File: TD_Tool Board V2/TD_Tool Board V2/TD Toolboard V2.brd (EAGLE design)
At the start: 8.6 x 5 mm, 142 parts, among them J3 430450400CON_430450400_MOL, M1 NMOSFET_WSD3066DN33, M2 CJ3400, M3 CJ3400, M4 CJ3400, P1 TPS54202_BUCKCONV, P2 3.3V, U1 RP2040IC57_RP2040-L, U2 W25Q128JVSIQSOIC_128JVSIQ_WIN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, U3 SN65HVD1050DRD8-L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

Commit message: Buck Converter Routing
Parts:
- moved 24V 128.3 mm to (92.2, -44.0)
- moved 5V 128.2 mm to (92.2, -41.8)
- moved R8 100.6 mm to (109.4, -43.4), turned to 0 degrees
- moved R9 99.6 mm to (109.4, -42.0), turned to 180 degrees
- moved R7 92.7 mm to (110.9, -44.6), turned to 0 degrees
- moved C21 46.2 mm to (111.7, -39.4), turned to 90 degrees
- moved J1 44.6 mm to (97.6, -43.9), turned to 90 degrees
- moved C22 43.4 mm to (111.8, -42.5), turned to 90 degrees
- moved C19 42.7 mm to (100.1, -42.2), turned to 90 degrees
- moved L1 42.6 mm to (105.9, -36.3), turned to 0 degrees
- moved C18 41.1 mm to (101.5, -42.3), turned to 90 degrees
- moved R6 41.0 mm to (102.7, -40.8), turned to 90 degrees
- moved R5 38.7 mm to (102.6, -44.4), turned to 90 degrees
- moved P1 36.0 mm to (106.3, -42.7), turned to 0 degrees
- moved C20 34.9 mm to (108.5, -40.7), turned to 0 degrees
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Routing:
- net GND: track 0.00 -> 35.6 mm, vias 0 -> 4
- net +5V: track 0.00 -> 15.7 mm
- net +24V: track 0.00 -> 15.7 mm
- net VREGO: track 0.00 -> 14.0 mm, vias 0 -> 8
- net VREGEN: track 0.00 -> 10.1 mm, vias 0 -> 3
- net VREGFB: track 0.00 -> 3.90 mm
- net VRC: track 0.00 -> 2.93 mm
- net BCBOOT: track 0.00 -> 1.13 mm
- added copper zone on layer 1, net +24V
- added copper zone on layer 1, net GND
- added copper zone on layer 1, net VREGO
- added copper zone on layer 16, net VREGO

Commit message: Buck Changed Finalised
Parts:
- moved GND 174.4 mm to (92.3, -42.3)
- moved 5V 1.28 mm to (92.3, -40.5)
- moved 24V 0.20 mm to (92.3, -44.2)
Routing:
- net +5V: track 15.7 -> 35.2 mm
- net VREGO: track 14.0 -> 17.9 mm, vias 8 -> 9
- net GND: track 35.6 -> 39.2 mm
- net +24V: track 15.7 -> 19.0 mm

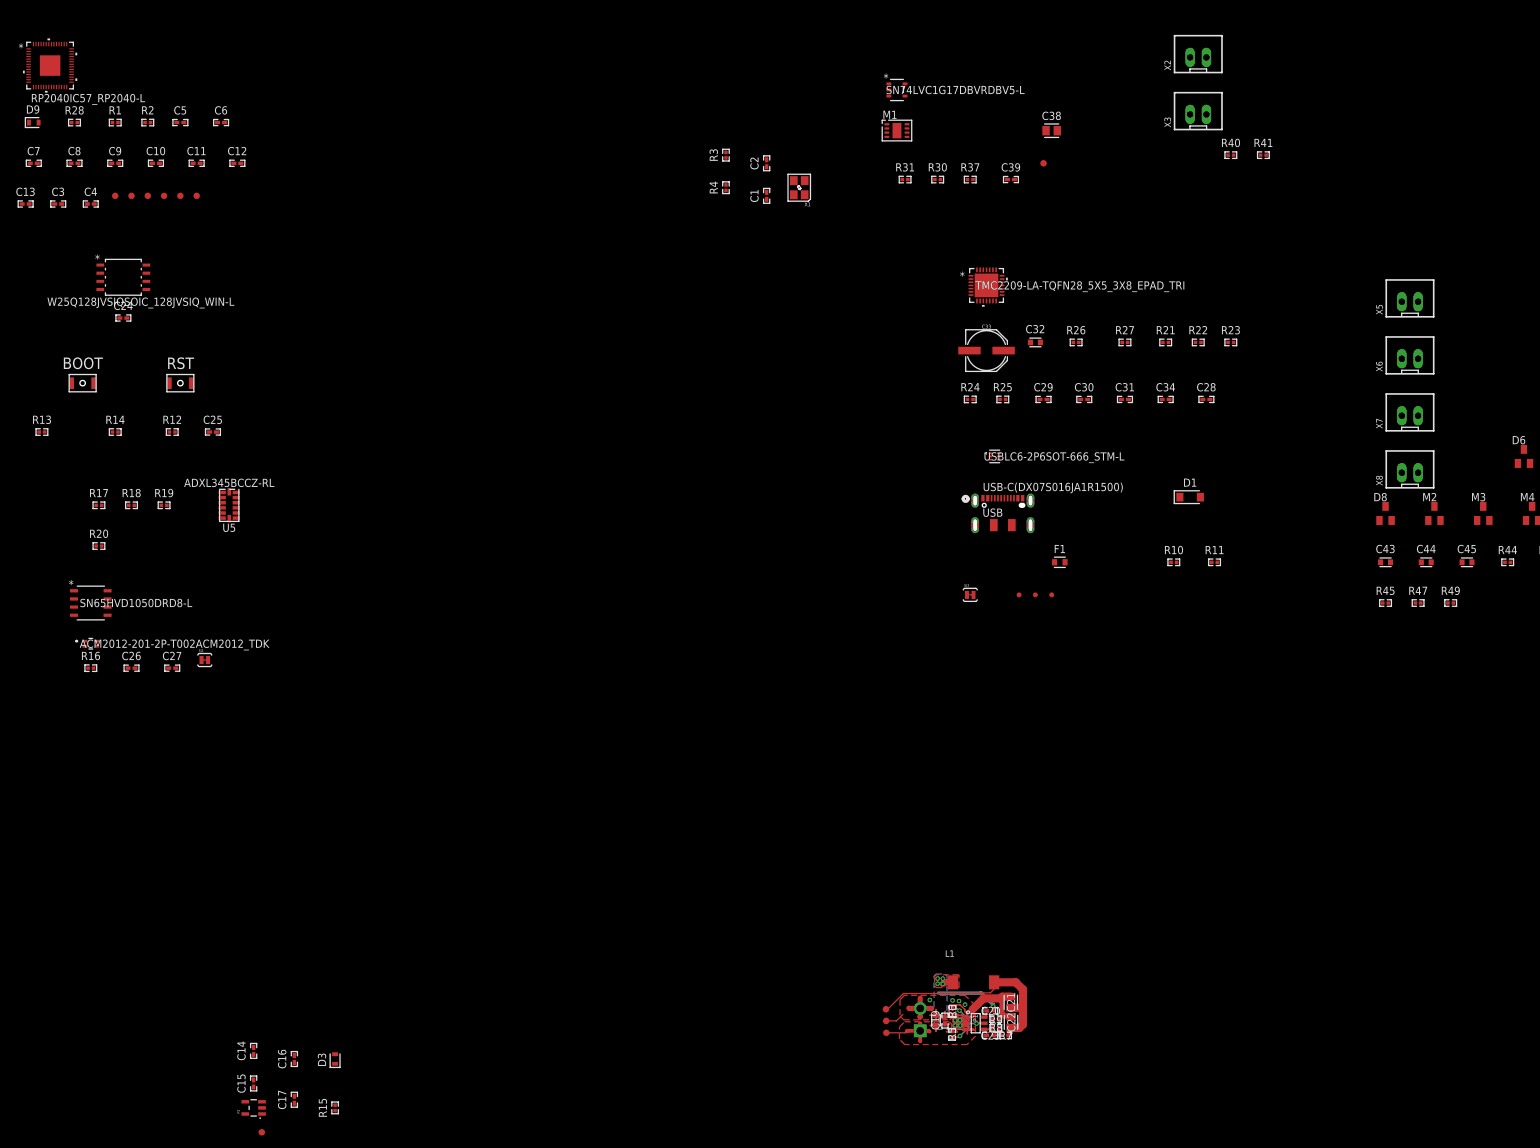
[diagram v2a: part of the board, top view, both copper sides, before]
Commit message: Added LDO Components
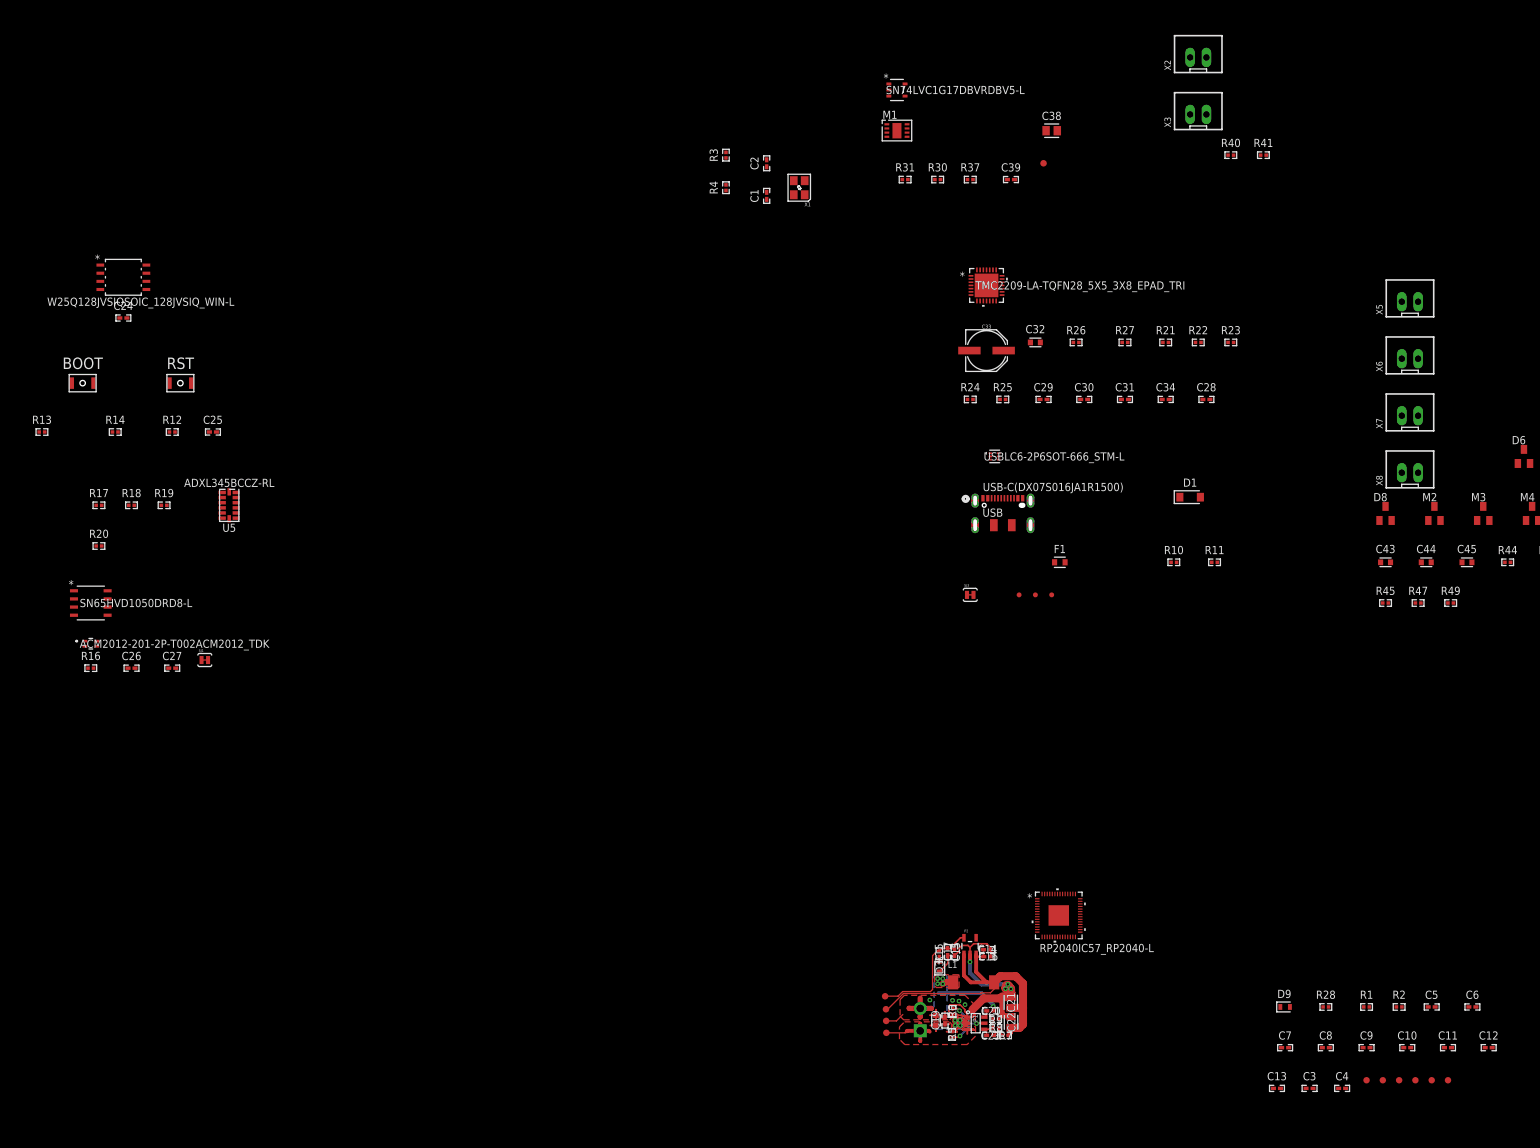
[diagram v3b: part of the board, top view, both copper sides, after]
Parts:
- moved C10 239.0 mm to (173.6, -46.5)
- moved C11 239.0 mm to (179.9, -46.5)
- moved C12 239.0 mm to (186.3, -46.5)
- moved C3 239.0 mm to (158.3, -52.8)
- moved C6 239.0 mm to (183.7, -40.1)
- moved C7 239.0 mm to (154.5, -46.5)
- moved D9 239.0 mm to (154.5, -40.1)
- moved FD2 239.0 mm to (169.8, -51.6)
- moved FD3 239.0 mm to (172.3, -51.6)
- moved FD6 239.0 mm to (179.9, -51.6)
- moved R2 239.0 mm to (172.3, -40.1)
- moved C13 239.0 mm to (153.2, -52.8)
- moved C4 239.0 mm to (163.4, -52.8)
- moved C5 239.0 mm to (177.4, -40.1)
- moved C8 239.0 mm to (160.9, -46.5)
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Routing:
- net GND: track 39.2 -> 65.2 mm, vias 4 -> 8
- net +3.3V: track 0.00 -> 19.6 mm
- net +5V: track 35.2 -> 52.5 mm
- net LDOLED: track 0.00 -> 0.85 mm
- added copper zone on layer 16, net GND

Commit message: Made Changes
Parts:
- moved U2 166.6 mm to (111.4, -19.6)
- moved C24 138.2 mm to (93.4, -1.12)
- moved C12 74.4 mm to (116.9, -19.5), turned to 90 degrees
- moved C5 70.6 mm to (108.0, -27.1), turned to 180 degrees
- moved C6 67.1 mm to (116.8, -36.7), turned to 270 degrees
- moved C11 63.0 mm to (117.7, -36.7), turned to 270 degrees
- moved C10 61.9 mm to (117.8, -19.5), turned to 90 degrees
- moved R11 54.4 mm to (119.9, -19.7), turned to 270 degrees
- moved C4 54.1 mm to (120.8, -19.5), turned to 90 degrees
- moved R10 52.3 mm to (118.8, -19.7), turned to 270 degrees
- moved C3 49.5 mm to (121.8, -19.5), turned to 90 degrees
- moved C9 49.3 mm to (124.3, -22.2)
- moved C8 43.3 mm to (124.3, -23.2)
- moved C7 35.5 mm to (124.4, -27.7)
- moved U1 4.97 mm to (115.4, -29.0)
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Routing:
- net +5V: track 52.5 -> 56.4 mm, vias 0 -> 6
- net VREGO: track 17.9 -> 21.4 mm
- added copper zone on layer 1, net +5V
- added copper zone on layer 16, net +5V

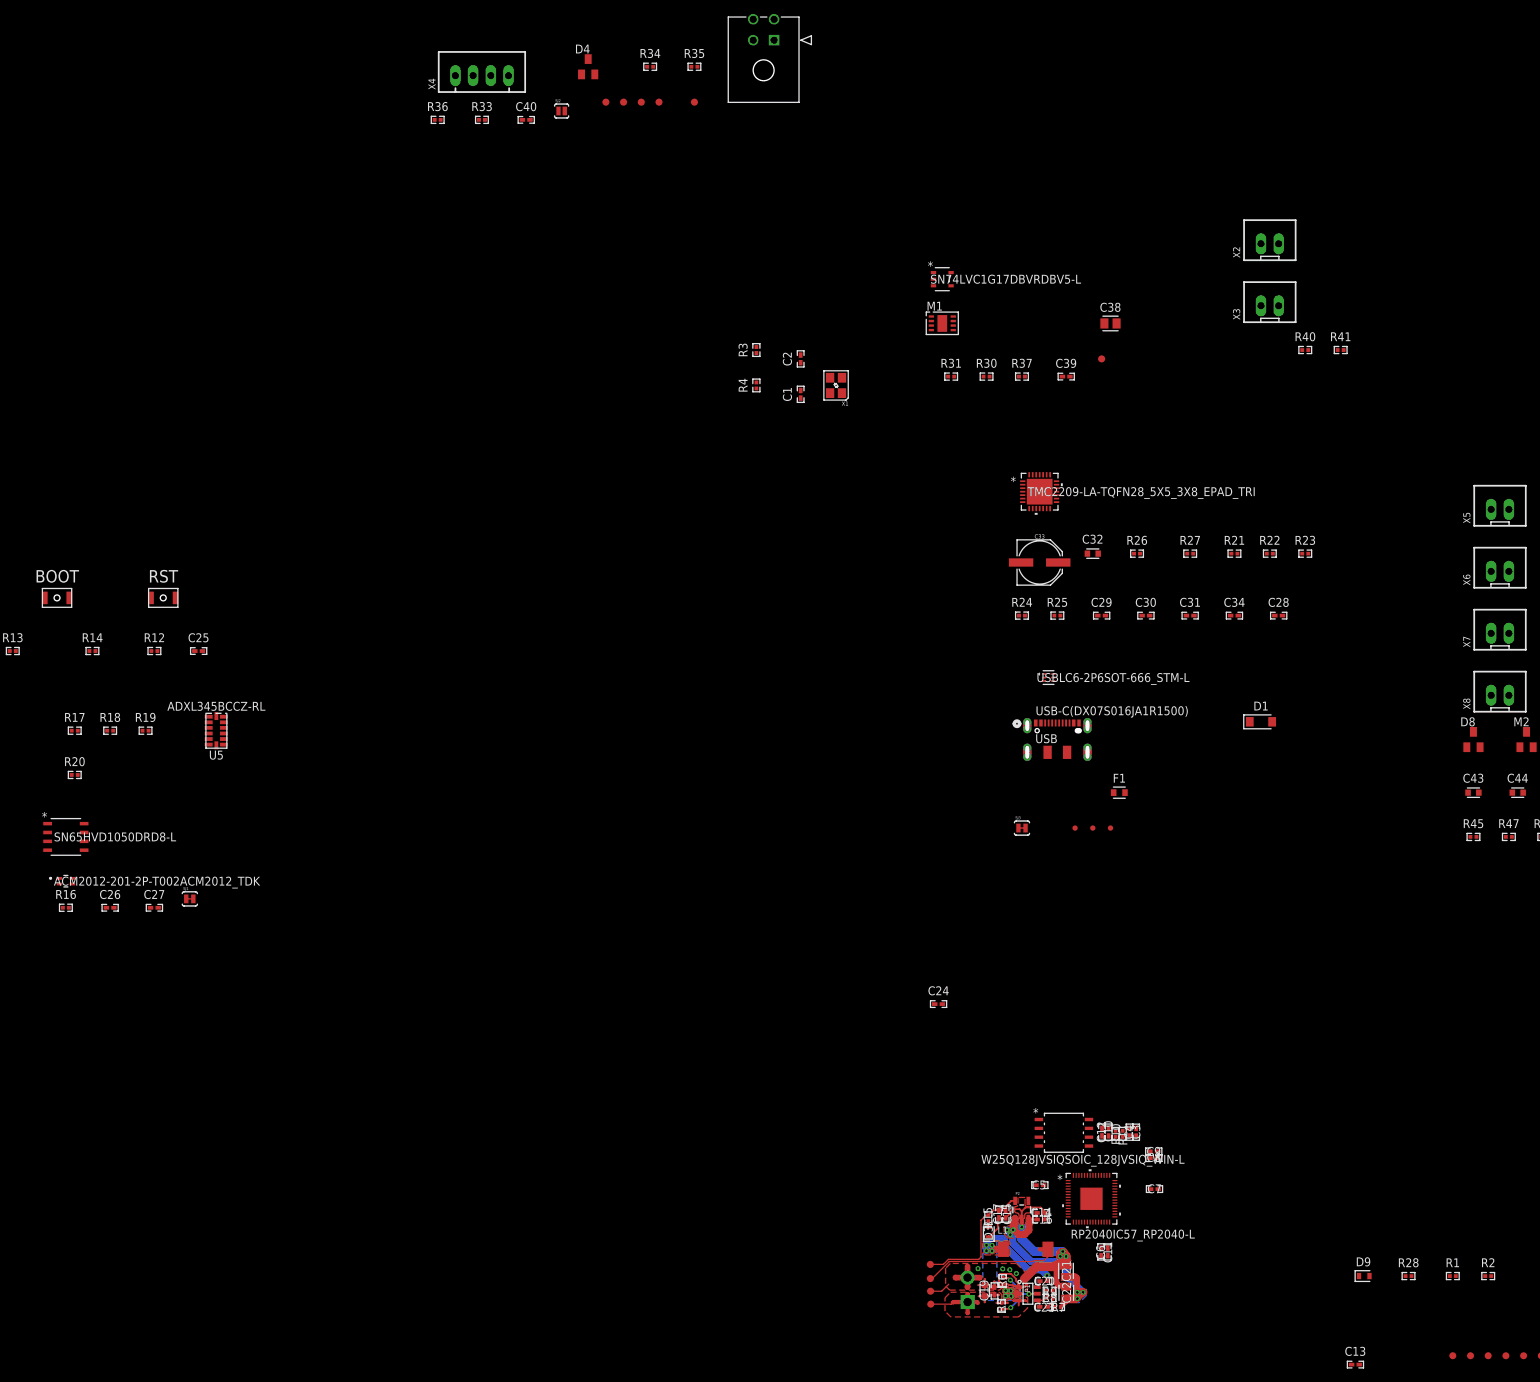
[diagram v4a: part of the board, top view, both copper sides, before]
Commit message: Routed most of the componenets to RP2040, Driver and GPIs remianing
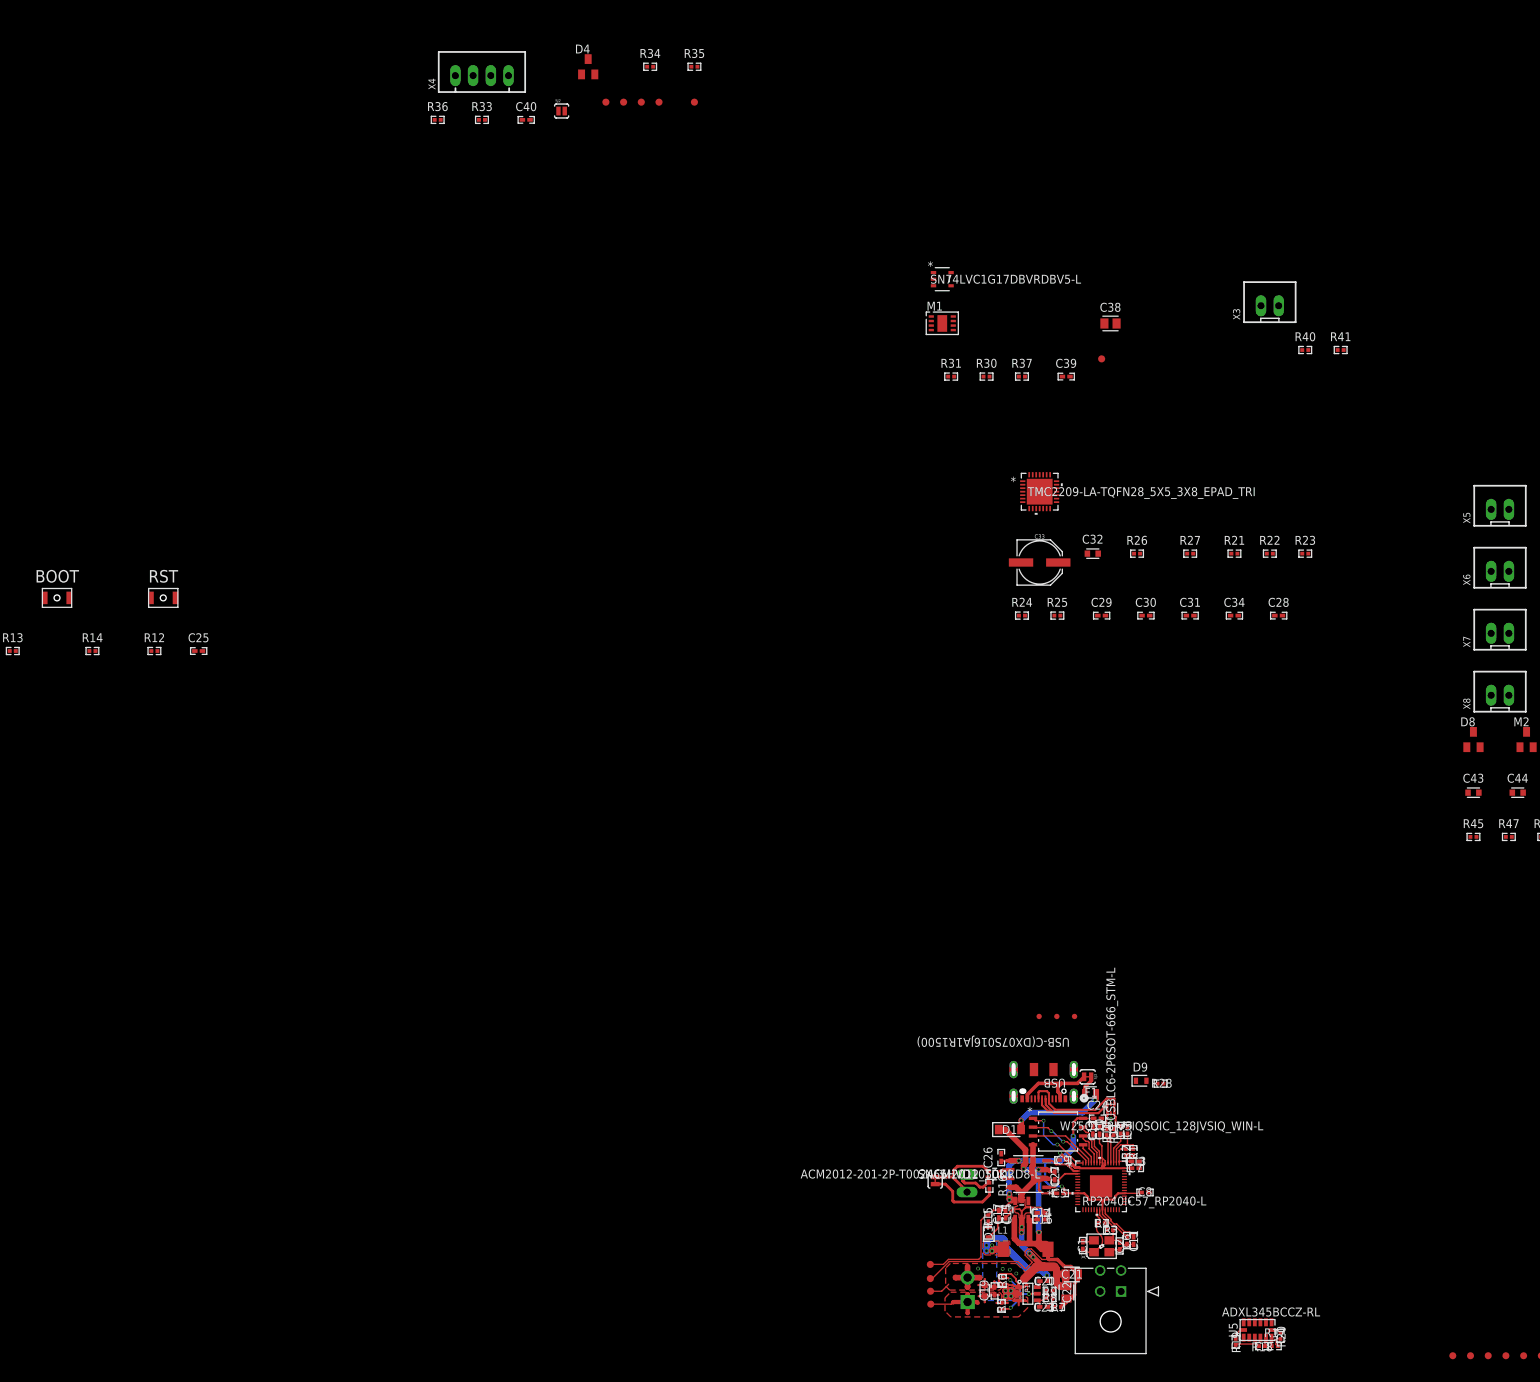
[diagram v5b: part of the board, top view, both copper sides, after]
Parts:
- moved R17 193.5 mm to (141.7, -50.2)
- moved R20 190.8 mm to (142.5, -48.7), turned to 270 degrees
- moved R18 187.4 mm to (139.9, -50.2), turned to 180 degrees
- moved J3 186.3 mm to (119.6, -42.3)
- moved R19 179.3 mm to (136.1, -49.6), turned to 270 degrees
- moved U5 172.4 mm to (139.2, -47.9), turned to 270 degrees
- moved U3 146.3 mm to (106.3, -25.5), turned to 180 degrees
- moved X2 141.6 mm to (97.5, -26.8), flipped to the bottom, turned to 270 degrees
- moved L2 139.7 mm to (101.5, -25.5), turned to 180 degrees
- moved R16 138.4 mm to (100.7, -27.2), turned to 270 degrees
- moved R3 136.1 mm to (118.0, -33.6), turned to 180 degrees
- moved C2 135.2 mm to (119.4, -35.8)
- moved C27 134.8 mm to (110.1, -25.8), turned to 270 degrees
- moved C26 132.8 mm to (102.4, -23.1), turned to 90 degrees
- moved R4 130.0 mm to (116.9, -32.5), turned to 180 degrees
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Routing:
- net +3.3V: track 19.3 -> 107.6 mm, vias 0 -> 6
- net GND: track 64.9 -> 90.8 mm
- net USB1_N: track 0.00 -> 19.1 mm
- net +5V: track 56.4 -> 74.9 mm, vias 6 -> 3
- net USB1_P: track 0.00 -> 17.3 mm
- net +1.1V: track 0.00 -> 15.3 mm
- net VBUS3: track 0.00 -> 14.3 mm, vias 0 -> 2
- net VBUS: track 0.00 -> 12.4 mm
- net CAN_N: track 0.00 -> 12.4 mm
- net QSPI_SS: track 0.00 -> 11.0 mm, vias 0 -> 2
- net CNT: track 0.00 -> 10.9 mm
- net QSPI_SD1: track 0.00 -> 9.94 mm, vias 0 -> 2
- net QSPI_SD2: track 0.00 -> 9.92 mm
- net OSC_IN: track 0.00 -> 8.41 mm
- net CAN_P: track 0.00 -> 6.55 mm
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- removed copper zone on layer 1, net +5V
- removed copper zone on layer 16, net +5V
- removed copper zone on layer 16, net GND
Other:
- outline, holes or cut-outs redrawn
